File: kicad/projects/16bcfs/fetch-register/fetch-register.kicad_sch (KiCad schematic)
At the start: 116 parts, among them J1 InstrReg, J10 Address Bus 2, J11 ALU Bus B, J12 Main Bus, J13 Control Signals, J14 Power, J15 Power, J2 MemBus1, J3 Address Bus 2, J4 ALU Bus B, J5 Main Bus, J6 Control Signals, J7 Power, J8 InstrReg, J9 MemBus1, U1 74HC541, U10 74HC541, U11 74HC574, U12 74HC574, U13 74HC541, U2 74HC541, U3 74HC541, U4 74HC541, U5 74HC541, U6 74HC541, U7 74HC541, U8 74HC541, U9 74HC541

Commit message: Draft a first update to the Fetch Reg Schematic
Here I take a first cut at updating the the Fetch Register Schematic.

No checks have been completed, just component renames and reductions.

A complete audit against the code is still required.
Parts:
- removed D17: Red, LED_SMD:LED_1206_3216Metric_Pad1.42x1.75mm_HandSolder, symbol Device:LED
- removed J1: InstrReg, Connector_PinSocket_2.54mm:PinSocket_1x16_P2.54mm_Vertical, symbol Connector:Conn_01x16_Socket
- removed J15: Power, Connector_PinHeader_2.54mm:PinHeader_1x02_P2.54mm_Vertical, symbol Connector:Conn_01x02_Pin
- removed J2: MemBus1, Connector_PinSocket_2.54mm:PinSocket_1x16_P2.54mm_Vertical, symbol Connector:Conn_01x16_Socket
- removed J3: Address Bus 2, Connector_PinSocket_2.54mm:PinSocket_1x16_P2.54mm_Vertical, symbol Connector:Conn_01x16_Socket
- removed J4: ALU Bus B, Connector_PinSocket_2.54mm:PinSocket_1x16_P2.54mm_Vertical, symbol Connector:Conn_01x16_Socket
- removed J5: Main Bus, Connector_PinSocket_2.54mm:PinSocket_1x16_P2.54mm_Vertical, symbol Connector:Conn_01x16_Socket
- removed J6: Control Signals, Connector_PinSocket_2.54mm:PinSocket_1x05_P2.54mm_Vertical, symbol Connector:Conn_01x05_Socket
- removed J7: Power, Connector_PinSocket_2.54mm:PinSocket_1x02_P2.54mm_Vertical, symbol Connector:Conn_01x02_Socket
- removed R49: 1K, Resistor_SMD:R_1206_3216Metric_Pad1.30x1.75mm_HandSolder, symbol Device:R
- removed U11, U12: 74HC574, Package_SO:SOIC-20W_7.5x12.8mm_P1.27mm, symbol eryjus:74AHC574
- added U11: 74HC04, symbol 74xx:74HC04
- J13: symbol Connector:Conn_01x05_Pin -> Connector:Conn_01x10_Pin
- J8: value InstrReg -> InstrRegInput
- J9: value MemBus1 -> FetchBusInput
- R1, R10, R11, R12, R13, R14, R15, R16, R17, R18, R19, R2, R20, R21, R22, R23, R24, R25, R26, R28, R3, R30, R32, R34, R36, R38, R4, R5, R6, R7, R8, R9: value 1K -> 10K; symbol Device:R -> Device:R_US
- R27, R29, R31, R33, R35, R37, R39, R40, R41, R42, R43, R44, R45, R46, R47, R48, R50, R51, R52, R53: symbol Device:R -> Device:R_US
- U1: value 74HC541 -> 74HC574; symbol eryjus:74AHC541 -> eryjus:74HC574; VarName (none) -> instRegBus1
- U10: value 74HC541 -> 74HC574; symbol eryjus:74AHC541 -> eryjus:74HC574; VarName (none) -> led0
- U13: symbol eryjus:74AHC541 -> eryjus:74HC541
- U2: value 74HC541 -> 74HC574; symbol eryjus:74AHC541 -> eryjus:74HC574; VarName (none) -> main1
- U3: value 74HC541 -> 74HC574; symbol eryjus:74AHC541 -> eryjus:74HC574; VarName (none) -> instrRegBus0
- U4: value 74HC541 -> 74HC574; symbol eryjus:74AHC541 -> eryjus:74HC574; VarName (none) -> main0
- U5: value 74HC541 -> 74HC574; symbol eryjus:74AHC541 -> eryjus:74HC574; VarName (none) -> addr21
- U6: value 74HC541 -> 74HC574; symbol eryjus:74AHC541 -> eryjus:74HC574; VarName (none) -> aluB1
- U7: value 74HC541 -> 74HC574; symbol eryjus:74AHC541 -> eryjus:74HC574; VarName (none) -> addr20
- U8: value 74HC541 -> 74HC574; symbol eryjus:74AHC541 -> eryjus:74HC574; VarName (none) -> aluB0
- U9: value 74HC541 -> 74HC574; symbol eryjus:74AHC541 -> eryjus:74HC574; VarName (none) -> led1
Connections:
- net Latch LED is gone; now on net Main LED: U13.18 (Y0)
- net RegBit0 is gone; now on net MemBus1Bit0: U10.9 (D7), U3.9 (D7), U4.9 (D7), U7.9 (D7), U8.9 (D7)
- net RegBit1 is gone; now on net MemBus1Bit1: U10.8 (D6), U3.8 (D6), U4.8 (D6), U7.8 (D6), U8.8 (D6)
- net RegBit2 is gone; now on net MemBus1Bit2: U10.7 (D5), U3.7 (D5), U4.7 (D5), U7.7 (D5), U8.7 (D5)
- net RegBit3 is gone; now on net MemBus1Bit3: U10.6 (D4), U3.6 (D4), U4.6 (D4), U7.6 (D4), U8.6 (D4)
- net RegBit4 is gone; now on net MemBus1Bit4: U10.5 (D3), U3.5 (D3), U4.5 (D3), U7.5 (D3), U8.5 (D3)
- net RegBit5 is gone; now on net MemBus1Bit5: U10.4 (D2), U3.4 (D2), U4.4 (D2), U7.4 (D2), U8.4 (D2)
- net RegBit6 is gone; now on net MemBus1Bit6: U10.3 (D1), U3.3 (D1), U4.3 (D1), U7.3 (D1), U8.3 (D1)
- net RegBit7 is gone; now on net MemBus1Bit7: U10.2 (D0), U3.2 (D0), U4.2 (D0), U7.2 (D0), U8.2 (D0)
- net RegBit8 is gone; now on net MemBus1Bit8: U1.9 (D7), U2.9 (D7), U5.9 (D7), U6.9 (D7), U9.9 (D7)
- net RegBit9 is gone; now on net MemBus1Bit9: U1.8 (D6), U2.8 (D6), U5.8 (D6), U6.8 (D6), U9.8 (D6)
- net RegBitA is gone; now on net MemBus1BitA: U1.7 (D5), U2.7 (D5), U5.7 (D5), U6.7 (D5), U9.7 (D5)
- net RegBitB is gone; now on net MemBus1BitB: U1.6 (D4), U2.6 (D4), U5.6 (D4), U6.6 (D4), U9.6 (D4)
- net RegBitC is gone; now on net MemBus1BitC: U1.5 (D3), U2.5 (D3), U5.5 (D3), U6.5 (D3), U9.5 (D3)
- net RegBitD is gone; now on net MemBus1BitD: U1.4 (D2), U2.4 (D2), U5.4 (D2), U6.4 (D2), U9.4 (D2)
- net RegBitE is gone; now on net MemBus1BitE: U1.3 (D1), U2.3 (D1), U5.3 (D1), U6.3 (D1), U9.3 (D1)
- net RegBitF is gone; now on net MemBus1BitF: U1.2 (D0), U2.2 (D0), U5.2 (D0), U6.2 (D0), U9.2 (D0)
- net ALU B LED: now also U13.17 (Y1); no longer U13.16 (Y2)
- net ALUBAssert: now also J13.4 (Pin_4), U13.3 (A1), U11.3; no longer J13.3 (Pin_3), U13.4 (A2), U6.19 (G2), U8.19 (G2)
- net ALUBBit0: now also U8.12 (Q7); no longer U8.11 (Y7)
- net ALUBBit1: now also U8.13 (Q6); no longer U8.12 (Y6)
- net ALUBBit2: now also U8.14 (Q5); no longer U8.13 (Y5)
- net ALUBBit3: now also U8.15 (Q4); no longer U8.14 (Y4)
- net ALUBBit4: now also U8.16 (Q3); no longer U8.15 (Y3)
- net ALUBBit5: now also U8.17 (Q2); no longer U8.16 (Y2)
- net ALUBBit6: now also U8.18 (Q1); no longer U8.17 (Y1)
- net ALUBBit7: now also U8.19 (Q0); no longer U8.18 (Y0)
- net ALUBBit8: now also U6.12 (Q7); no longer U6.11 (Y7)
- net ALUBBit9: now also U6.13 (Q6); no longer U6.12 (Y6)
- net ALUBBitA: now also U6.14 (Q5); no longer U6.13 (Y5)
- net ALUBBitB: now also U6.15 (Q4); no longer U6.14 (Y4)
- net ALUBBitC: now also U6.16 (Q3); no longer U6.15 (Y3)
- net ALUBBitD: now also U6.17 (Q2); no longer U6.16 (Y2)
- net ALUBBitE: now also U6.18 (Q1); no longer U6.17 (Y1)
- net ALUBBitF: now also U6.19 (Q0); no longer U6.18 (Y0)
- net AddrBus2 LED: now also U13.15 (Y3); no longer U13.14 (Y4)
- net AddrBus2Assert: now also U13.5 (A3), U11.5; no longer U13.6 (A4), U5.19 (G2), U7.19 (G2)
- net AddrBus2Bit0: now also U7.12 (Q7); no longer U7.11 (Y7)
- net AddrBus2Bit1: now also U7.13 (Q6); no longer U7.12 (Y6)
- net AddrBus2Bit2: now also U7.14 (Q5); no longer U7.13 (Y5)
- net AddrBus2Bit3: now also U7.15 (Q4); no longer U7.14 (Y4)
- net AddrBus2Bit4: now also U7.16 (Q3); no longer U7.15 (Y3)
- net AddrBus2Bit5: now also U7.17 (Q2); no longer U7.16 (Y2)
- net AddrBus2Bit6: now also U7.18 (Q1); no longer U7.17 (Y1)
- net AddrBus2Bit7: now also U7.19 (Q0); no longer U7.18 (Y0)
- net AddrBus2Bit8: now also U5.12 (Q7); no longer U5.11 (Y7)
- net AddrBus2Bit9: now also U5.13 (Q6); no longer U5.12 (Y6)
- net AddrBus2BitA: now also U5.14 (Q5); no longer U5.13 (Y5)
- net AddrBus2BitB: now also U5.15 (Q4); no longer U5.14 (Y4)
- net AddrBus2BitC: now also U5.16 (Q3); no longer U5.15 (Y3)
- net AddrBus2BitD: now also U5.17 (Q2); no longer U5.16 (Y2)
- net AddrBus2BitE: now also U5.18 (Q1); no longer U5.17 (Y1)
- net AddrBus2BitF: now also U5.19 (Q0); no longer U5.18 (Y0)
- net Bit 0 LED: now also U10.12 (Q7); no longer U10.11 (Y7)
- net Bit 1 LED: now also U10.13 (Q6); no longer U10.12 (Y6)
- net Bit 2 LED: now also U10.14 (Q5); no longer U10.13 (Y5)
- net Bit 3 LED: now also U10.15 (Q4); no longer U10.14 (Y4)
- net Bit 4 LED: now also U10.16 (Q3); no longer U10.15 (Y3)
- net Bit 5 LED: now also U10.17 (Q2); no longer U10.16 (Y2)
- net Bit 6 LED: now also U10.18 (Q1); no longer U10.17 (Y1)
- net Bit 7 LED: now also U10.19 (Q0); no longer U10.18 (Y0)
- net Bit 8 LED: now also U9.12 (Q7); no longer U9.11 (Y7)
- net Bit 9 LED: now also U9.13 (Q6); no longer U9.12 (Y6)
- net Bit A LED: now also U9.14 (Q5); no longer U9.13 (Y5)
- net Bit B LED: now also U9.15 (Q4); no longer U9.14 (Y4)
- net Bit C LED: now also U9.16 (Q3); no longer U9.15 (Y3)
- net Bit D LED: now also U9.17 (Q2); no longer U9.16 (Y2)
- net Bit E LED: now also U9.18 (Q1); no longer U9.17 (Y1)
- net Bit F LED: now also U9.19 (Q0); no longer U9.18 (Y0)
- net GNDREF: now also J13.10 (Pin_10), J13.2 (Pin_2), U13.6 (A4), U11.11, U11.13, U11.7 (GND), U11.9; no longer U1.1 (G1), U10.19 (G2), U2.1 (G1), U3.1 (G1), U4.1 (G1), U5.1 (G1), U6.1 (G1), U7.1 (G1), U8.1 (G1), U9.19 (G2)
- net InstrReg LED: now also U13.16 (Y2); no longer U13.15 (Y3)
- net InstrRegBit0: now also U3.12 (Q7); no longer U3.11 (Y7)
- net InstrRegBit1: now also U3.13 (Q6); no longer U3.12 (Y6)
- net InstrRegBit2: now also U3.14 (Q5); no longer U3.13 (Y5)
- net InstrRegBit3: now also U3.15 (Q4); no longer U3.14 (Y4)
- net InstrRegBit4: now also U3.16 (Q3); no longer U3.15 (Y3)
- net InstrRegBit5: now also U3.17 (Q2); no longer U3.16 (Y2)
- net InstrRegBit6: now also U3.18 (Q1); no longer U3.17 (Y1)
- net InstrRegBit7: now also U3.19 (Q0); no longer U3.18 (Y0)
- net InstrRegBit8: now also U1.12 (Q7); no longer U1.11 (Y7)
- net InstrRegBit9: now also U1.13 (Q6); no longer U1.12 (Y6)
- net InstrRegBitA: now also U1.14 (Q5); no longer U1.13 (Y5)
- net InstrRegBitB: now also U1.15 (Q4); no longer U1.14 (Y4)
- net InstrRegBitC: now also U1.16 (Q3); no longer U1.15 (Y3)
- net InstrRegBitD: now also U1.17 (Q2); no longer U1.16 (Y2)
- net InstrRegBitE: now also U1.18 (Q1); no longer U1.17 (Y1)
- net InstrRegBitF: now also U1.19 (Q0); no longer U1.18 (Y0)
- net InstrRegSuppress: now also J13.6 (Pin_6), U1.1 (OE), U13.4 (A2), U3.1 (OE); no longer J13.4 (Pin_4), U1.19 (G2), U13.5 (A3), U3.19 (G2)
- net Main LED: no longer U13.17 (Y1)
- net MainBit0: now also U4.12 (Q7); no longer U4.11 (Y7)
- net MainBit1: now also U4.13 (Q6); no longer U4.12 (Y6)
- net MainBit2: now also U4.14 (Q5); no longer U4.13 (Y5)
- net MainBit3: now also U4.15 (Q4); no longer U4.14 (Y4)
- net MainBit4: now also U4.16 (Q3); no longer U4.15 (Y3)
- net MainBit5: now also U4.17 (Q2); no longer U4.16 (Y2)
- net MainBit6: now also U4.18 (Q1); no longer U4.17 (Y1)
- net MainBit7: now also U4.19 (Q0); no longer U4.18 (Y0)
- net MainBit8: now also U2.12 (Q7); no longer U2.11 (Y7)
- net MainBit9: now also U2.13 (Q6); no longer U2.12 (Y6)
- net MainBitA: now also U2.14 (Q5); no longer U2.13 (Y5)
- net MainBitB: now also U2.15 (Q4); no longer U2.14 (Y4)
- net MainBitC: now also U2.16 (Q3); no longer U2.15 (Y3)
- net MainBitD: now also U2.17 (Q2); no longer U2.16 (Y2)
- net MainBitE: now also U2.18 (Q1); no longer U2.17 (Y1)
- net MainBitF: now also U2.19 (Q0); no longer U2.18 (Y0)
- net MainBusAssert: now also J13.3 (Pin_3), U13.2 (A0), U11.1; no longer J13.2 (Pin_2), U13.3 (A1), U2.19 (G2), U4.19 (G2)
- net MemBus1Bit0: no longer J9.1 (Pin_1)
- net MemBus1Bit1: no longer J9.2 (Pin_2)
- net MemBus1Bit2: no longer J9.3 (Pin_3)
- net MemBus1Bit3: no longer J9.4 (Pin_4)
- net MemBus1Bit4: no longer J9.5 (Pin_5)
- net MemBus1Bit5: no longer J9.6 (Pin_6)
- net MemBus1Bit6: no longer J9.7 (Pin_7)
- net MemBus1Bit7: no longer J9.8 (Pin_8)
- net MemBus1Bit8: no longer J9.9 (Pin_9)
- net MemBus1Bit9: no longer J9.10 (Pin_10)
- net MemBus1BitA: no longer J9.11 (Pin_11)
- net MemBus1BitB: no longer J9.12 (Pin_12)
- net MemBus1BitC: no longer J9.13 (Pin_13)
- net MemBus1BitD: no longer J9.14 (Pin_14)
- net MemBus1BitE: no longer J9.15 (Pin_15)
- net MemBus1BitF: no longer J9.16 (Pin_16)
- net VCC: now also J13.9 (Pin_9), U11.14 (VCC)
- net RawCLK renamed CpuClk
- net CpuClk: now also U1.11 (Cp), U10.11 (Cp), U2.11 (Cp), U3.11 (Cp), U4.11 (Cp), U5.11 (Cp), U6.11 (Cp), U7.11 (Cp), U8.11 (Cp), U9.11 (Cp); no longer U13.2 (A0)
- new net FetchBusBit0: J9.1 (Pin_1)
- new net FetchBusBit1: J9.2 (Pin_2)
- new net FetchBusBit2: J9.3 (Pin_3)
- new net FetchBusBit3: J9.4 (Pin_4)
- new net FetchBusBit4: J9.5 (Pin_5)
- new net FetchBusBit5: J9.6 (Pin_6)
- new net FetchBusBit6: J9.7 (Pin_7)
- new net FetchBusBit7: J9.8 (Pin_8)
- new net FetchBusBit8: J9.9 (Pin_9)
- new net FetchBusBit9: J9.10 (Pin_10)
- new net FetchBusBitA: J9.11 (Pin_11)
- new net FetchBusBitB: J9.12 (Pin_12)
- new net FetchBusBitC: J9.13 (Pin_13)
- new net FetchBusBitD: J9.14 (Pin_14)
- new net FetchBusBitE: J9.15 (Pin_15)
- new net FetchBusBitF: J9.16 (Pin_16)
- new net Reset: J13.7 (Pin_7)
- new net ~{ALU B Assert}: U11.4, U6.1 (OE), U8.1 (OE)
- new net ~{Addr 2 Assert}: U11.6, U5.1 (OE), U7.1 (OE)
- new net ~{Main Assert}: U11.2, U2.1 (OE), U4.1 (OE)
- new net ~{RHLD}: J13.8 (Pin_8)
- no-connect marks 3 -> 7
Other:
- moved on the sheet: C1, C10, C11, C12, C13, C14, C2, C3, C4, C5, C6, C7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

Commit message: Update the Fetch Register Schematics
This commit updates the Fetch Register Schematics to reflect the new
design.  As far as I can tell at the time of this commit, all changes
are properly reflected and no other changes are expected, except maybe
adding a test point or 2 as the situation on the PCB dictates.
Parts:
- removed C12: 0.1uF, Capacitor_SMD:C_1206_3216Metric_Pad1.33x1.80mm_HandSolder, symbol Device:C_Polarized_US
- C12: renamed from C13; value 0.1uF -> 47uF
- renumbered C14 to C13, D18 to D17, D19 to D18, D20 to D19, D21 to D20, J8 to J1, J11 to J2, J9 to J3, J12 to J4, J13 to J5, J10 to J6, J14 to J7, R27 to R1, R42 to R10, R43 to R11, R44 to R12, R45 to R13, R46 to R14, R47 to R15, R48 to R16, R50 to R17, R51 to R18, R52 to R19, R29 to R2, R53 to R20, R1 to R21, R2 to R22, R3 to R23, R4 to R24, R5 to R25, R6 to R26, R7 to R27, R8 to R28, R9 to R29, R31 to R3, R10 to R30, R11 to R31, R12 to R32, R13 to R33, R14 to R34, R15 to R35, R16 to R36, R17 to R37, R18 to R38, R19 to R39, R33 to R4, R20 to R40, R21 to R41, R22 to R42, R23 to R43, R24 to R44, R25 to R45, R26 to R46, R28 to R47, R30 to R48, R32 to R49, R35 to R5, R34 to R50, R36 to R51, R38 to R52, R37 to R6, R39 to R7, R40 to R8, R41 to R9, U5 to U1, U6 to U10, U8 to U11, U13 to U12, U7 to U2, U1 to U3, U3 to U4, U9 to U5, U10 to U6, U11 to U7, U2 to U8, U4 to U9
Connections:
- net MemBus1Bit0 is gone; now on net FetchBusBit0: R37.1, U11.9 (D7), U2.9 (D7), U4.9 (D7), U6.9 (D7), U9.9 (D7)
- net MemBus1Bit1 is gone; now on net FetchBusBit1: R38.1, U11.8 (D6), U2.8 (D6), U4.8 (D6), U6.8 (D6), U9.8 (D6)
- net MemBus1Bit2 is gone; now on net FetchBusBit2: R39.1, U11.7 (D5), U2.7 (D5), U4.7 (D5), U6.7 (D5), U9.7 (D5)
- net MemBus1Bit3 is gone; now on net FetchBusBit3: R40.1, U11.6 (D4), U2.6 (D4), U4.6 (D4), U6.6 (D4), U9.6 (D4)
- net MemBus1Bit4 is gone; now on net FetchBusBit4: R41.1, U11.5 (D3), U2.5 (D3), U4.5 (D3), U6.5 (D3), U9.5 (D3)
- net MemBus1Bit5 is gone; now on net FetchBusBit5: R42.1, U11.4 (D2), U2.4 (D2), U4.4 (D2), U6.4 (D2), U9.4 (D2)
- net MemBus1Bit6 is gone; now on net FetchBusBit6: R43.1, U11.3 (D1), U2.3 (D1), U4.3 (D1), U6.3 (D1), U9.3 (D1)
- net MemBus1Bit7 is gone; now on net FetchBusBit7: R44.1, U11.2 (D0), U2.2 (D0), U4.2 (D0), U6.2 (D0), U9.2 (D0)
- net MemBus1Bit8 is gone; now on net FetchBusBit8: R45.1, U1.9 (D7), U10.9 (D7), U3.9 (D7), U5.9 (D7), U8.9 (D7)
- net MemBus1Bit9 is gone; now on net FetchBusBit9: R46.1, U1.8 (D6), U10.8 (D6), U3.8 (D6), U5.8 (D6), U8.8 (D6)
- net MemBus1BitA is gone; now on net FetchBusBitA: R47.1, U1.7 (D5), U10.7 (D5), U3.7 (D5), U5.7 (D5), U8.7 (D5)
- net MemBus1BitB is gone; now on net FetchBusBitB: R48.1, U1.6 (D4), U10.6 (D4), U3.6 (D4), U5.6 (D4), U8.6 (D4)
- net MemBus1BitC is gone; now on net FetchBusBitC: R49.1, U1.5 (D3), U10.5 (D3), U3.5 (D3), U5.5 (D3), U8.5 (D3)
- net MemBus1BitD is gone; now on net FetchBusBitD: R50.1, U1.4 (D2), U10.4 (D2), U3.4 (D2), U5.4 (D2), U8.4 (D2)
- net MemBus1BitE is gone; now on net FetchBusBitE: R51.1, U1.3 (D1), U10.3 (D1), U3.3 (D1), U5.3 (D1), U8.3 (D1)
- net MemBus1BitF is gone; now on net FetchBusBitF: R52.1, U1.2 (D0), U10.2 (D0), U3.2 (D0), U5.2 (D0), U8.2 (D0)
- no-connect marks 7 -> 9
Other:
- note added: "ALU Bus B Assert"
- note added: "Address Bus 2 Assert"
- note added: "Assert to Instruction Register"
- note added: "Contents LEDs"
- note added: "Main Bus Assert"
- note added: "Power & Decoupling"
- note added: "Pull-Down Resistors"
- note added: "Register Inputs/Outputs"
- note added: "Signal LED Driver"
- note added: "Signal Shaping"
- note added: "Unused"
- moved on the sheet: C1, C10, C11, C12, C13, C2, C3, C4, C5, C6, C7, C8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

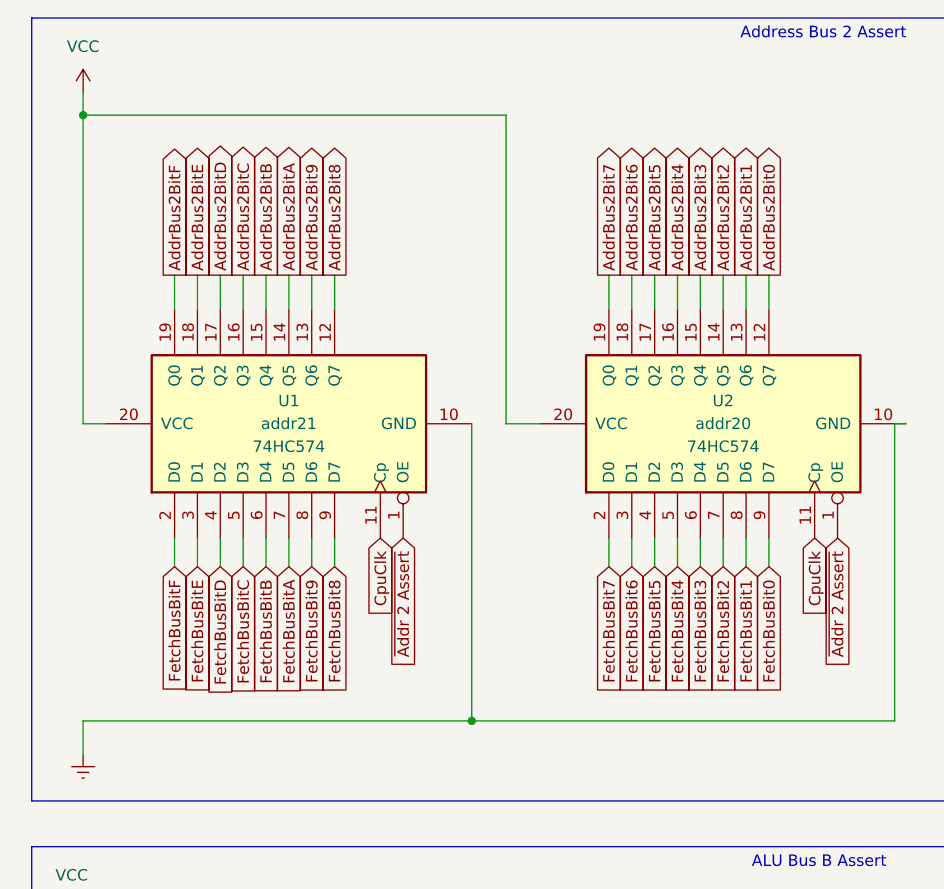
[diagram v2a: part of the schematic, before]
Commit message: Update the big-picture component placement
For the Fetch Register, all components needed to be removed and
re-placed into the PCB.  This commit is a first cut at that placement to
try to arrange the PCB.  The PCB can be shrunk quite a bit (maybe by
25%?) and this commit preceeds those changes.

Some changes were made to the schematic in order to drive more
efficient trace routing.
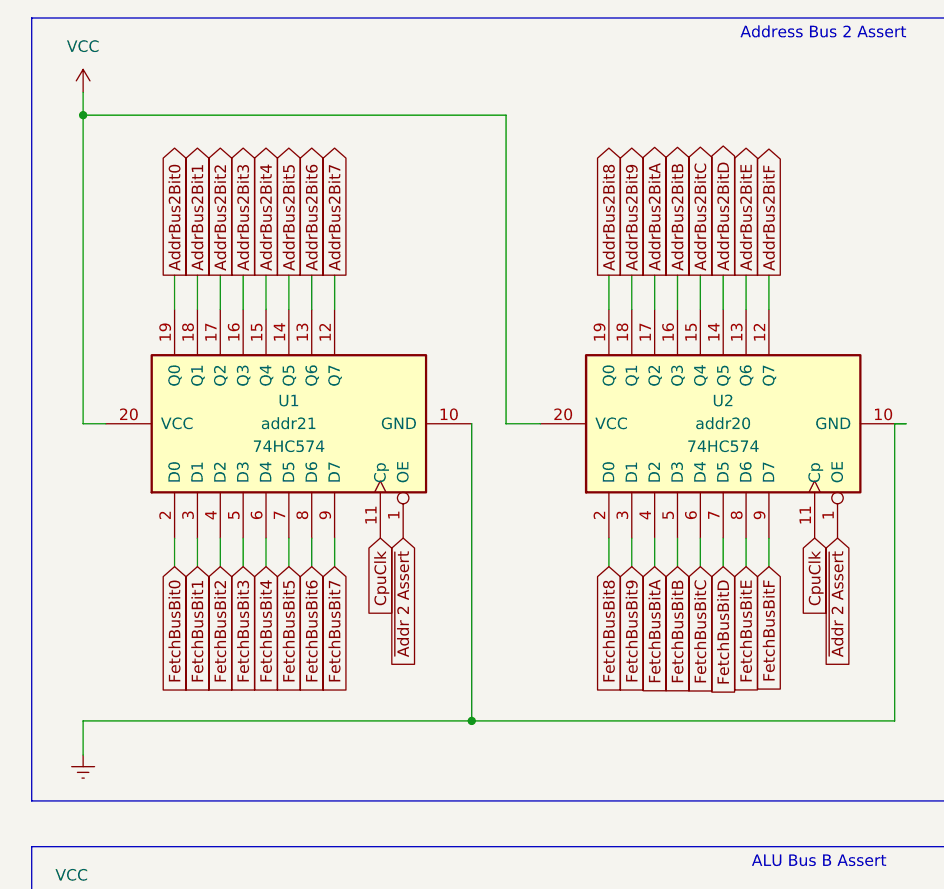
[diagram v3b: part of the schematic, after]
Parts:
- J5: footprint Connector_PinHeader_2.54mm:PinHeader_1x05_P2.54mm_Vertical -> Connector_PinHeader_2.54mm:PinHeader_1x10_P2.54mm_Vertical
- U7: footprint (none) -> Package_SO:SOIC-14_3.9x8.7mm_P1.27mm
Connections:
- net AddrBus2Bit0: now also U1.19 (Q0); no longer U2.12 (Q7)
- net AddrBus2Bit1: now also U1.18 (Q1); no longer U2.13 (Q6)
- net AddrBus2Bit2: now also U1.17 (Q2); no longer U2.14 (Q5)
- net AddrBus2Bit3: now also U1.16 (Q3); no longer U2.15 (Q4)
- net AddrBus2Bit4: now also U1.15 (Q4); no longer U2.16 (Q3)
- net AddrBus2Bit5: now also U1.14 (Q5); no longer U2.17 (Q2)
- net AddrBus2Bit6: now also U1.13 (Q6); no longer U2.18 (Q1)
- net AddrBus2Bit7: now also U1.12 (Q7); no longer U2.19 (Q0)
- net AddrBus2Bit8: now also U2.19 (Q0); no longer U1.12 (Q7)
- net AddrBus2Bit9: now also U2.18 (Q1); no longer U1.13 (Q6)
- net AddrBus2BitA: now also U2.17 (Q2); no longer U1.14 (Q5)
- net AddrBus2BitB: now also U2.16 (Q3); no longer U1.15 (Q4)
- net AddrBus2BitC: now also U2.15 (Q4); no longer U1.16 (Q3)
- net AddrBus2BitD: now also U2.14 (Q5); no longer U1.17 (Q2)
- net AddrBus2BitE: now also U2.13 (Q6); no longer U1.18 (Q1)
- net AddrBus2BitF: now also U2.12 (Q7); no longer U1.19 (Q0)
- net FetchBusBit0: now also U1.2 (D0); no longer U2.9 (D7)
- net FetchBusBit1: now also U1.3 (D1); no longer U2.8 (D6)
- net FetchBusBit2: now also U1.4 (D2); no longer U2.7 (D5)
- net FetchBusBit3: now also U1.5 (D3); no longer U2.6 (D4)
- net FetchBusBit4: now also U1.6 (D4); no longer U2.5 (D3)
- net FetchBusBit5: now also U1.7 (D5); no longer U2.4 (D2)
- net FetchBusBit6: now also U1.8 (D6); no longer U2.3 (D1)
- net FetchBusBit7: now also U1.9 (D7); no longer U2.2 (D0)
- net FetchBusBit8: now also U2.2 (D0); no longer U1.9 (D7)
- net FetchBusBit9: now also U2.3 (D1); no longer U1.8 (D6)
- net FetchBusBitA: now also U2.4 (D2); no longer U1.7 (D5)
- net FetchBusBitB: now also U2.5 (D3); no longer U1.6 (D4)
- net FetchBusBitC: now also U2.6 (D4); no longer U1.5 (D3)
- net FetchBusBitD: now also U2.7 (D5); no longer U1.4 (D2)
- net FetchBusBitE: now also U2.8 (D6); no longer U1.3 (D1)
- net FetchBusBitF: now also U2.9 (D7); no longer U1.2 (D0)
